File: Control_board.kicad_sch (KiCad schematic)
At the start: 34 parts, among them IC1 CNY74-2H, IC2 CNY74-2H, J1 Conn_01x02_Pin, K1 SR11-3V-200-2C, K2 SR5-12V-200-1C, U1 Teensy4.1, U2 01530007Z, U3 01530007Z

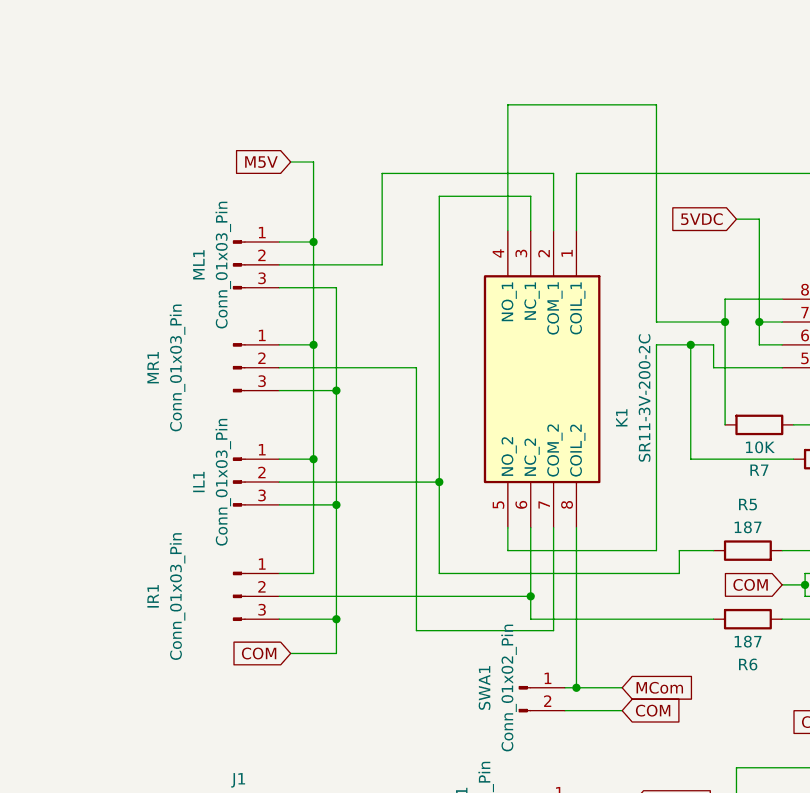
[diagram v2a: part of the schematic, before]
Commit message: Swapped Signal and 5+
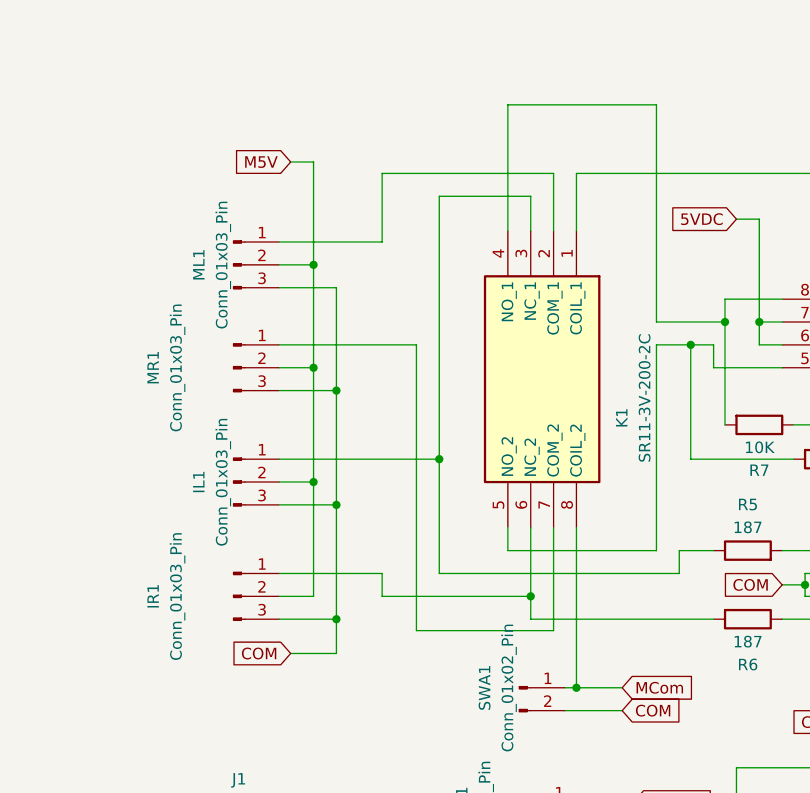
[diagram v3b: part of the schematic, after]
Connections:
- net M5V: now also IL1.2 (Pin_2), IR1.2 (Pin_2), ML1.2 (Pin_2), MR1.2 (Pin_2); no longer IL1.1 (Pin_1), IR1.1 (Pin_1), ML1.1 (Pin_1), MR1.1 (Pin_1)
- net at K1.3 (NC_1), R5.1: now also IL1.1 (Pin_1); no longer IL1.2 (Pin_2)
- net at K1.6 (NC_2), R6.2: now also IR1.1 (Pin_1); no longer IR1.2 (Pin_2)
- net at K1.2 (COM_1): now also ML1.1 (Pin_1); no longer ML1.2 (Pin_2)
- net at K1.7 (COM_2): now also MR1.1 (Pin_1); no longer MR1.2 (Pin_2)
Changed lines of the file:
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@@
   (title_block
     (title "AGV Control Board")
-    (rev "V1.2")
-    (comment 1 "In/Out Swapped on A3C and A4C")
-    (comment 2 "*Adding redable Txt on board")
-    (comment 3 "E and C Swapped")
+    (rev "V1.3")
+    (comment 1 "Swapped Signal and 5+")
   )
   (junction (at 130.81 86.36) (diameter 0) (color 0 0 0 0)
   )
+  (junction (at 41.91 54.61) (diameter 0) (color 0 0 0 0)
+  )
   (junction (at 102.87 62.23) (diameter 0) (color 0 0 0 0)
   )
-  (junction (at 41.91 52.07) (diameter 0) (color 0 0 0 0)
-  )
   (junction (at 121.92 50.8) (diameter 0) (color 0 0 0 0)
   )
   (junction (at 217.17 27.94) (diameter 0) (color 0 0 0 0)
   )
-  (junction (at 55.88 67.31) (diameter 0) (color 0 0 0 0)
-  )
   (junction (at 224.79 31.75) (diameter 0) (color 0 0 0 0)
   )
-  (junction (at 41.91 40.64) (diameter 0) (color 0 0 0 0)
-  )
   (junction (at 252.73 27.94) (diameter 0) (color 0 0 0 0)
   )
+  (junction (at 41.91 43.18) (diameter 0) (color 0 0 0 0)
+  )
+  (junction (at 138.43 66.04) (diameter 0) (color 0 0 0 0)
+  )
+  (junction (at 138.43 33.02) (diameter 0) (color 0 0 0 0)
+  )
+  (junction (at 135.89 146.05) (diameter 0) (color 0 0 0 0)
+  )
+  (junction (at 96.52 78.74) (diameter 0) (color 0 0 0 0)
+  )
   (junction (at 66.04 80.01) (diameter 0) (color 0 0 0 0)
   )
-  (junction (at 138.43 66.04) (diameter 0) (color 0 0 0 0)
-  )
-  (junction (at 138.43 33.02) (diameter 0) (color 0 0 0 0)
-  )
-  (junction (at 135.89 146.05) (diameter 0) (color 0 0 0 0)
-  )
-  (junction (at 96.52 78.74) (diameter 0) (color 0 0 0 0)
-  )
   (junction (at 133.35 83.82) (diameter 0) (color 0 0 0 0)
   )
@@
   (junction (at 87.63 49.53) (diameter 0) (color 0 0 0 0)
   )
-  (junction (at 41.91 64.77) (diameter 0) (color 0 0 0 0)
-  )
   (junction (at 91.44 49.53) (diameter 0) (color 0 0 0 0)
   )
@@
   (junction (at 44.45 57.15) (diameter 0) (color 0 0 0 0)
   )
+  (junction (at 41.91 67.31) (diameter 0) (color 0 0 0 0)
+  )
   (junction (at 44.45 69.85) (diameter 0) (color 0 0 0 0)
   )
+  (junction (at 55.88 64.77) (diameter 0) (color 0 0 0 0)
+  )
   (junction (at 83.82 52.07) (diameter 0) (color 0 0 0 0)
   )
@@
     (stroke (width 0) (type default))
   )
-  (wire (pts (xy 38.1 40.64) (xy 41.91 40.64))
-    (stroke (width 0) (type default))
-  )
   (wire (pts (xy 234.95 78.74) (xy 234.95 111.76))
     (stroke (width 0) (type default))
@@
     (stroke (width 0) (type default))
   )
+  (wire (pts (xy 49.53 40.64) (xy 49.53 33.02))
+    (stroke (width 0) (type default))
+  )
   (wire (pts (xy 96.52 80.01) (xy 96.52 78.74))
     (stroke (width 0) (type default))
@@
     (stroke (width 0) (type default))
   )
+  (wire (pts (xy 38.1 67.31) (xy 41.91 67.31))
+    (stroke (width 0) (type default))
+  )
   (wire (pts (xy 87.63 46.99) (xy 87.63 49.53))
     (stroke (width 0) (type default))
@@
     (stroke (width 0) (type default))
   )
-  (wire (pts (xy 41.91 77.47) (xy 41.91 64.77))
+  (wire (pts (xy 38.1 40.64) (xy 49.53 40.64))
     (stroke (width 0) (type default))
   )
@@
     (stroke (width 0) (type default))
   )
-  (wire (pts (xy 41.91 40.64) (xy 41.91 52.07))
-    (stroke (width 0) (type default))
-  )
   (wire (pts (xy 100.33 113.03) (xy 107.95 113.03))
     (stroke (width 0) (type default))
@@
     (stroke (width 0) (type default))
   )
+  (wire (pts (xy 41.91 67.31) (xy 41.91 80.01))
+    (stroke (width 0) (type default))
+  )
   (wire (pts (xy 71.12 102.87) (xy 77.47 102.87))
     (stroke (width 0) (type default))
   )
+  (wire (pts (xy 66.04 80.01) (xy 66.04 82.55))
+    (stroke (width 0) (type default))
+  )
   (wire (pts (xy 80.01 74.93) (xy 63.5 74.93))
     (stroke (width 0) (type default))
@@
     (stroke (width 0) (type default))
   )
-  (wire (pts (xy 38.1 77.47) (xy 41.91 77.47))
-    (stroke (width 0) (type default))
-  )
   (wire (pts (xy 110.49 107.95) (xy 110.49 113.03))
     (stroke (width 0) (type default))
@@
     (stroke (width 0) (type default))
   )
-  (wire (pts (xy 66.04 80.01) (xy 66.04 82.55))
-    (stroke (width 0) (type default))
-  )
   (wire (pts (xy 55.88 134.62) (xy 60.96 134.62))
     (stroke (width 0) (type default))
@@
     (stroke (width 0) (type default))
   )
-  (wire (pts (xy 41.91 52.07) (xy 38.1 52.07))
-    (stroke (width 0) (type default))
-  )
   (wire (pts (xy 88.9 99.06) (xy 129.54 99.06))
     (stroke (width 0) (type default))
@@
     (stroke (width 0) (type default))
   )
+  (wire (pts (xy 38.1 54.61) (xy 41.91 54.61))
+    (stroke (width 0) (type default))
+  )
   (wire (pts (xy 124.46 74.93) (xy 133.35 74.93))
     (stroke (width 0) (type default))
@@
     (stroke (width 0) (type default))
   )
-  (wire (pts (xy 38.1 67.31) (xy 55.88 67.31))
-    (stroke (width 0) (type default))
-  )
   (wire (pts (xy 217.17 27.94) (xy 226.06 27.94))
     (stroke (width 0) (type default))
@@
     (stroke (width 0) (type default))
   )
+  (wire (pts (xy 41.91 43.18) (xy 41.91 54.61))
+    (stroke (width 0) (type default))
+  )
   (wire (pts (xy 130.81 54.61) (xy 130.81 63.5))
     (stroke (width 0) (type default))
@@
     (stroke (width 0) (type default))
   )
-  (wire (pts (xy 38.1 80.01) (xy 66.04 80.01))
-    (stroke (width 0) (type default))
-  )
   (wire (pts (xy 229.87 58.42) (xy 250.19 58.42))
     (stroke (width 0) (type default))
@@
     (stroke (width 0) (type default))
   )
-  (wire (pts (xy 55.88 77.47) (xy 55.88 67.31))
-    (stroke (width 0) (type default))
-  )
   (wire (pts (xy 93.98 49.53) (xy 91.44 49.53))
     (stroke (width 0) (type default))
@@
     (stroke (width 0) (type default))
   )
+  (wire (pts (xy 38.1 77.47) (xy 49.53 77.47))
+    (stroke (width 0) (type default))
+  )
   (wire (pts (xy 209.55 76.2) (xy 236.22 76.2))
     (stroke (width 0) (type default))
@@
     (stroke (width 0) (type default))
   )
-  (wire (pts (xy 49.53 43.18) (xy 49.53 33.02))
-    (stroke (width 0) (type default))
-  )
   (wire (pts (xy 86.36 82.55) (xy 66.04 82.55))
     (stroke (width 0) (type default))
@@
     (stroke (width 0) (type default))
   )
-  (wire (pts (xy 53.34 54.61) (xy 53.34 83.82))
-    (stroke (width 0) (type default))
-  )
   (wire (pts (xy 130.81 63.5) (xy 153.67 63.5))
     (stroke (width 0) (type default))
   )
+  (wire (pts (xy 55.88 64.77) (xy 55.88 77.47))
+    (stroke (width 0) (type default))
+  )
   (wire (pts (xy 39.37 86.36) (xy 44.45 86.36))
     (stroke (width 0) (type default))
@@
     (stroke (width 0) (type default))
   )
+  (wire (pts (xy 38.1 43.18) (xy 41.91 43.18))
+    (stroke (width 0) (type default))
+  )
   (wire (pts (xy 55.88 132.08) (xy 71.12 132.08))
     (stroke (width 0) (type default))
@@
     (stroke (width 0) (type default))
   )
-  (wire (pts (xy 38.1 54.61) (xy 53.34 54.61))
-    (stroke (width 0) (type default))
-  )
   (wire (pts (xy 55.88 139.7) (xy 71.12 139.7))
     (stroke (width 0) (type default))
@@
     (stroke (width 0) (type default))
   )
+  (wire (pts (xy 38.1 64.77) (xy 55.88 64.77))
+    (stroke (width 0) (type default))
+  )
   (wire (pts (xy 130.81 82.55) (xy 130.81 86.36))
     (stroke (width 0) (type default))
@@
     (stroke (width 0) (type default))
   )
-  (wire (pts (xy 41.91 31.75) (xy 41.91 40.64))
-    (stroke (width 0) (type default))
-  )
   (wire (pts (xy 240.03 31.75) (xy 246.38 31.75))
     (stroke (width 0) (type default))
@@
     (stroke (width 0) (type default))
   )
-  (wire (pts (xy 55.88 67.31) (xy 55.88 35.56))
+  (wire (pts (xy 55.88 35.56) (xy 55.88 64.77))
     (stroke (width 0) (type default))
   )
@@
     (stroke (width 0) (type default))
   )
+  (wire (pts (xy 41.91 54.61) (xy 41.91 67.31))
+    (stroke (width 0) (type default))
+  )
   (wire (pts (xy 138.43 33.02) (xy 71.12 33.02))
     (stroke (width 0) (type default))
   )
+  (wire (pts (xy 38.1 52.07) (xy 53.34 52.07))
+    (stroke (width 0) (type default))
+  )
+  (wire (pts (xy 49.53 80.01) (xy 66.04 80.01))
+    (stroke (width 0) (type default))
+  )
   (wire (pts (xy 55.88 137.16) (xy 60.96 137.16))
     (stroke (width 0) (type default))
@@
     (stroke (width 0) (type default))
   )
+  (wire (pts (xy 49.53 77.47) (xy 49.53 80.01))
+    (stroke (width 0) (type default))
+  )
   (wire (pts (xy 110.49 149.86) (xy 121.92 149.86))
     (stroke (width 0) (type default))
   )
-  (wire (pts (xy 66.04 80.01) (xy 66.04 72.39))
+  (wire (pts (xy 66.04 72.39) (xy 66.04 80.01))
+    (stroke (width 0) (type default))
+  )
+  (wire (pts (xy 53.34 52.07) (xy 53.34 83.82))
     (stroke (width 0) (type default))
   )
@@
     (stroke (width 0) (type default))
   )
-  (wire (pts (xy 38.1 43.18) (xy 49.53 43.18))
-    (stroke (width 0) (type default))
-  )
   (wire (pts (xy 44.45 86.36) (xy 44.45 82.55))
     (stroke (width 0) (type default))
@@
     (stroke (width 0) (type default))
   )
-  (wire (pts (xy 41.91 64.77) (xy 41.91 52.07))
+  (wire (pts (xy 41.91 31.75) (xy 41.91 43.18))
     (stroke (width 0) (type default))
   )
@@
     (stroke (width 0) (type default))
   )
-  (wire (pts (xy 38.1 64.77) (xy 41.91 64.77))
-    (stroke (width 0) (type default))
-  )
   (wire (pts (xy 93.98 74.93) (xy 99.06 74.93))
     (stroke (width 0) (type default))
@@
     (stroke (width 0) (type default))
   )
+  (wire (pts (xy 41.91 80.01) (xy 38.1 80.01))
+    (stroke (width 0) (type default))
+  )
